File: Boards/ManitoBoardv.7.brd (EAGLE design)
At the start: 81 x 73.7 mm, 44 parts, among them U1 BLUETOOTH-RN41", U2 ATMEGA328P

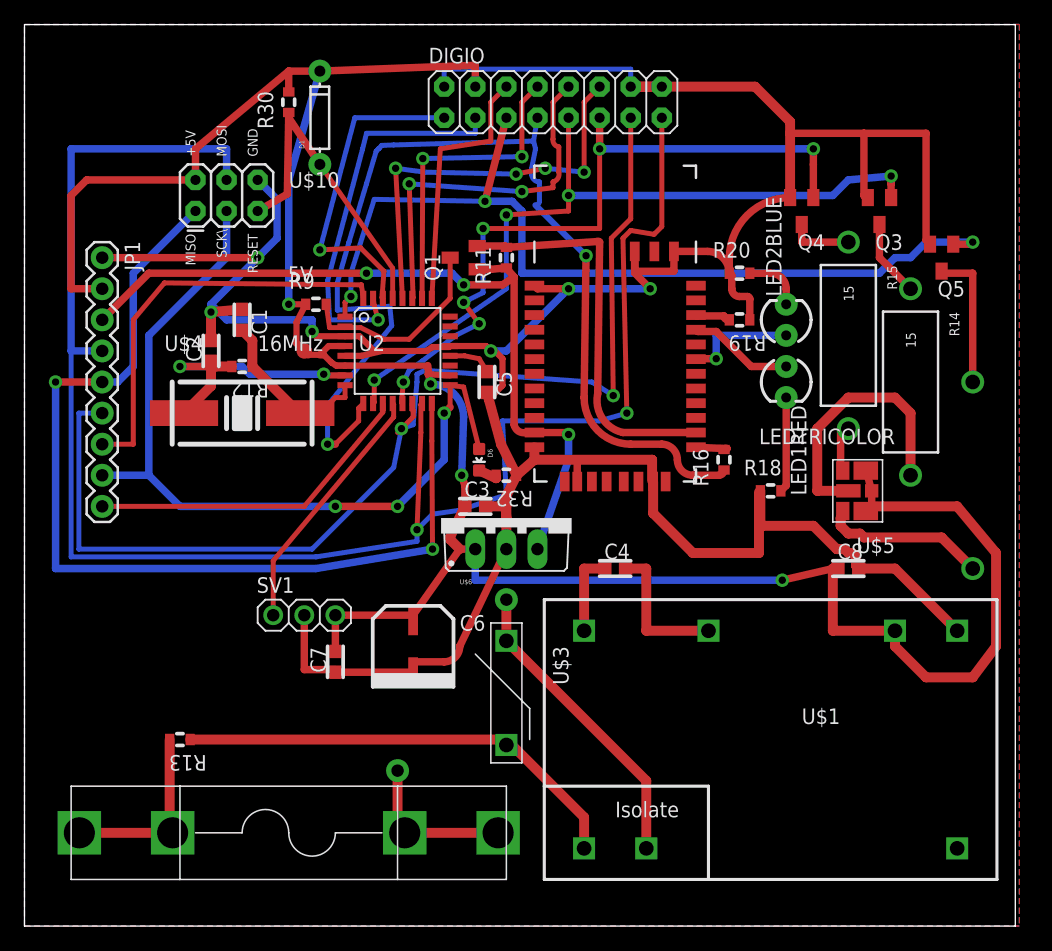
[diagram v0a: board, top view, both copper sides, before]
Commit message: IncompleteRevisions
Attempting to shrink board size, reduce variety of trace widths,
simplify angles, remove curved corners, improve thermal relief
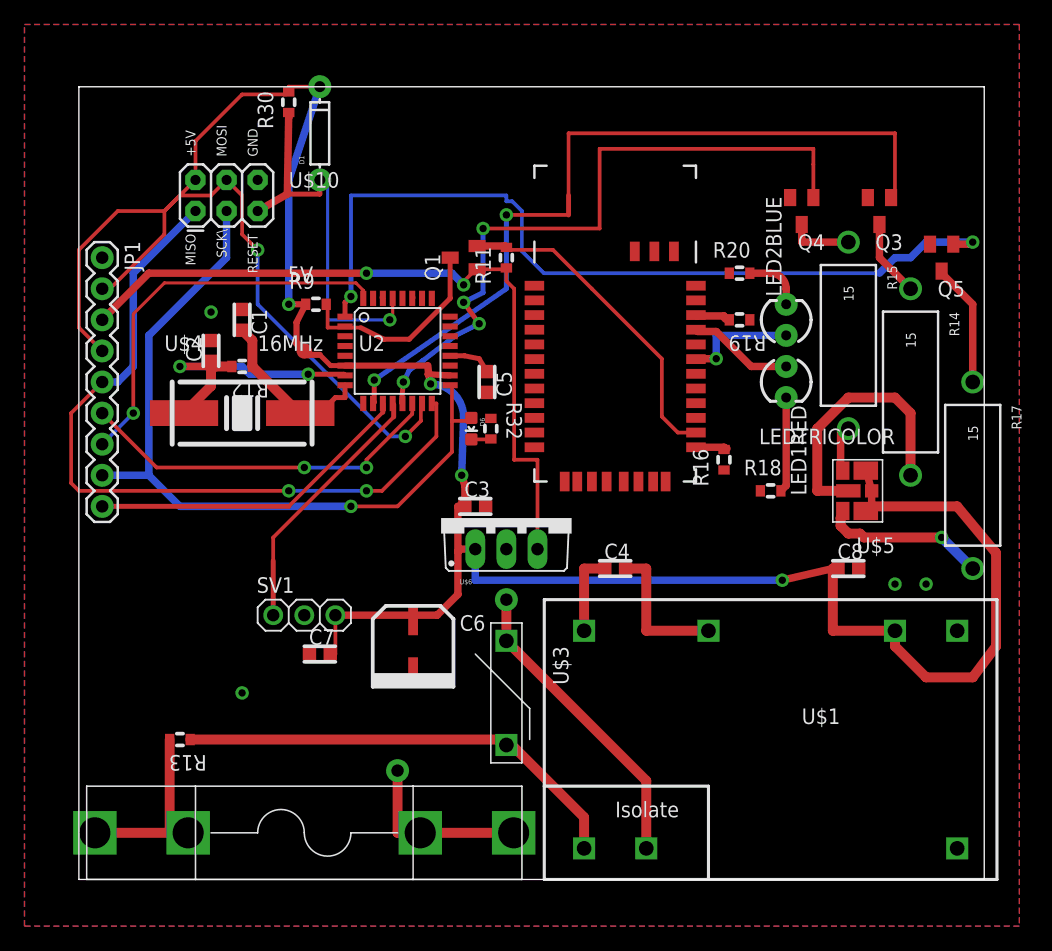
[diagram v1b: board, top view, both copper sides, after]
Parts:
- removed DIGIO: M08X2, CharlieCreations:2X8
- moved R32 4.02 mm to (57.1, 40.6), turned to 270 degrees
- moved D6 2.62 mm to (55.6, 40.6)
- moved C7 1.42 mm to (43.2, 22.2), turned to 0 degrees
- moved D1 1.27 mm to (43.2, 64.8)
- moved U$2 1.27 mm to (41.9, 7.62)
- flipped R17 to the top
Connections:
- net +5V: no longer DIGIO.4
- net AD2: no longer DIGIO.6
- net AD3: no longer DIGIO.8
- net GND: no longer DIGIO.14, DIGIO.16, DIGIO.2
- net IO0: no longer DIGIO.1
- net IO1: no longer DIGIO.3
- net IO10/SS: no longer DIGIO.13
- net IO11/MOSI: no longer DIGIO.15
- net IO3: no longer DIGIO.5
- net IO5/RX: no longer DIGIO.7
- net IO6: no longer DIGIO.9
- net IO9: no longer DIGIO.11
- net SCL/AD5: no longer DIGIO.12
- net SDA/AD4: no longer DIGIO.10
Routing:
- net GND: track 278.4 -> 0.00 mm, vias 6 -> 4
- net IO5/RX: track 88.2 -> 0.00 mm, vias 2 -> 0
- net IO11/MOSI: track 142.0 -> 54.5 mm
- net IO10/SS: track 92.6 -> 30.2 mm
- net SCL/AD5: track 33.6 -> 0.00 mm, vias 4 -> 0
- net IO1: track 31.6 -> 0.00 mm, vias 1 -> 0
- net SDA/AD4: track 30.3 -> 0.10 mm, vias 2 -> 0
- net IO0: track 26.8 -> 0.10 mm, vias 1 -> 0
- net AD3: track 25.8 -> 0.00 mm, vias 2 -> 0
- net +5V: track 204.6 -> 179.2 mm
- net AD2: track 21.4 -> 0.00 mm
- net IO12/MISO: track 79.7 -> 62.2 mm
- net IO3: track 74.1 -> 68.4 mm, vias 3 -> 2
- net RESET: track 27.3 -> 32.8 mm, vias 0 -> 1
- net TX: track 32.8 -> 27.7 mm
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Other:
- board size 81 x 73.7 mm -> 74 x 64.8 mm
